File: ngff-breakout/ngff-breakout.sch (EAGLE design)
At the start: 79 parts, among them U1 MIC5366-1.8YC5, U2 MCP1827S-3302E/EB, X1 PINHD-2X4, X10 ZX360D-B-10P(30), X2 692121030100, X3 PINHD-2X10, X4 PINHD-2X5, X5 694108106102, X6 PINHD-1X3, X7 5-1814832-1, X8 5-1814832-1, X9 5-1814832-1, Y1 MHF4, Y2 MHF4, Y3 MHF4

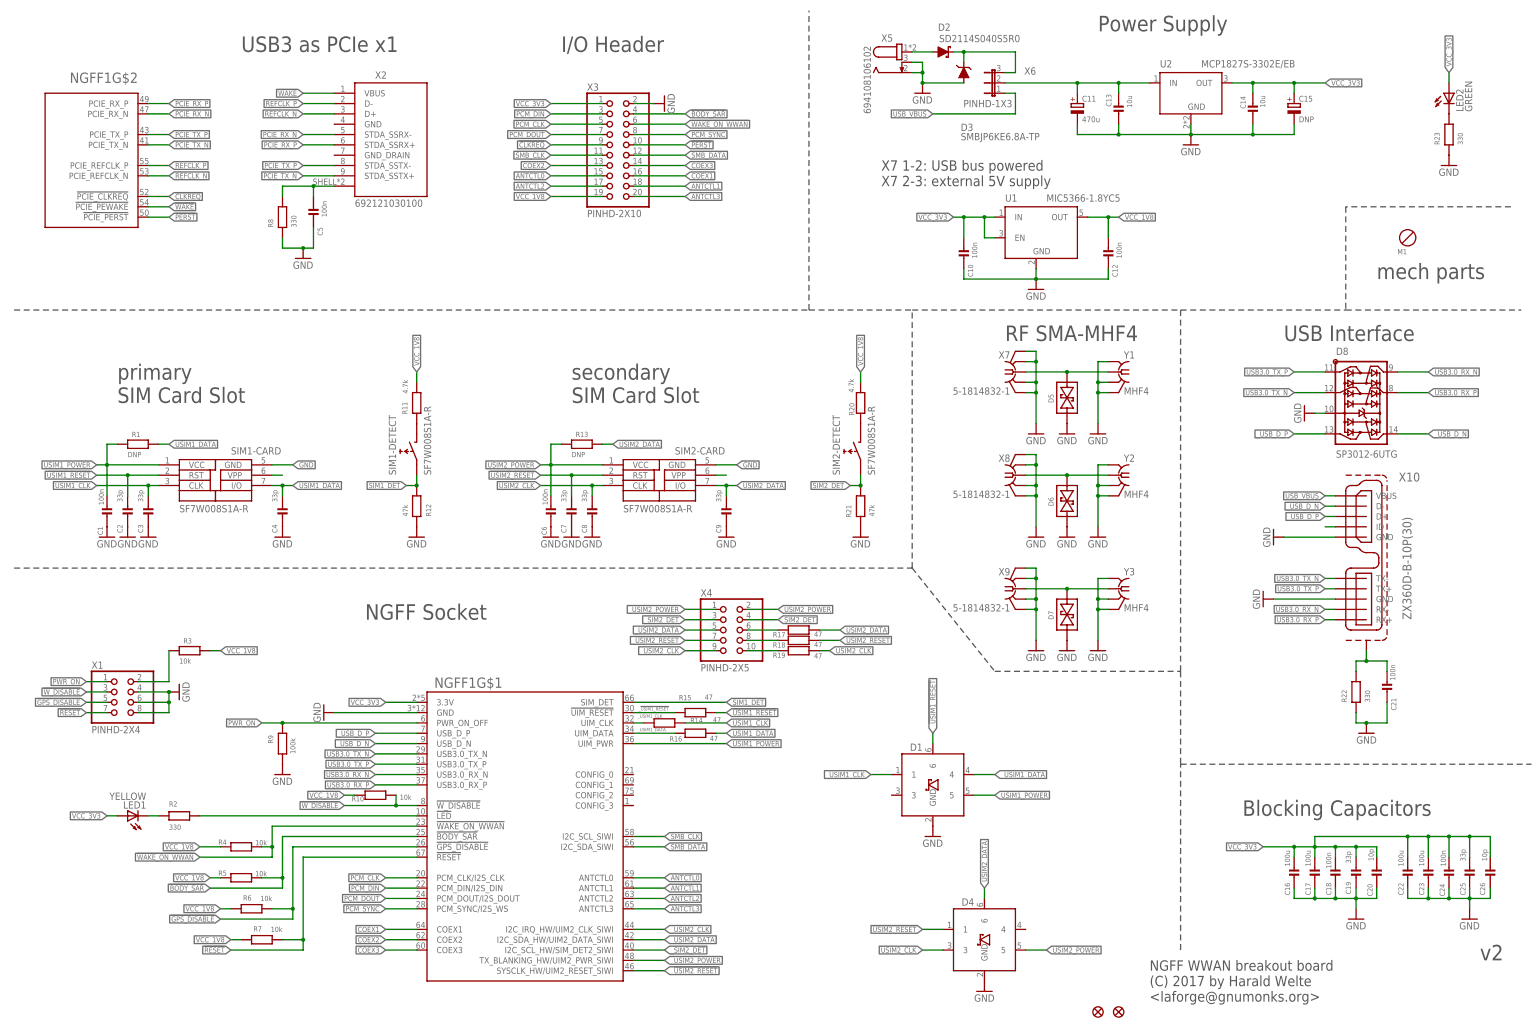
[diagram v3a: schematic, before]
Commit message: ngff: connect pin 4 @X2 to GND (solves OS#4216)
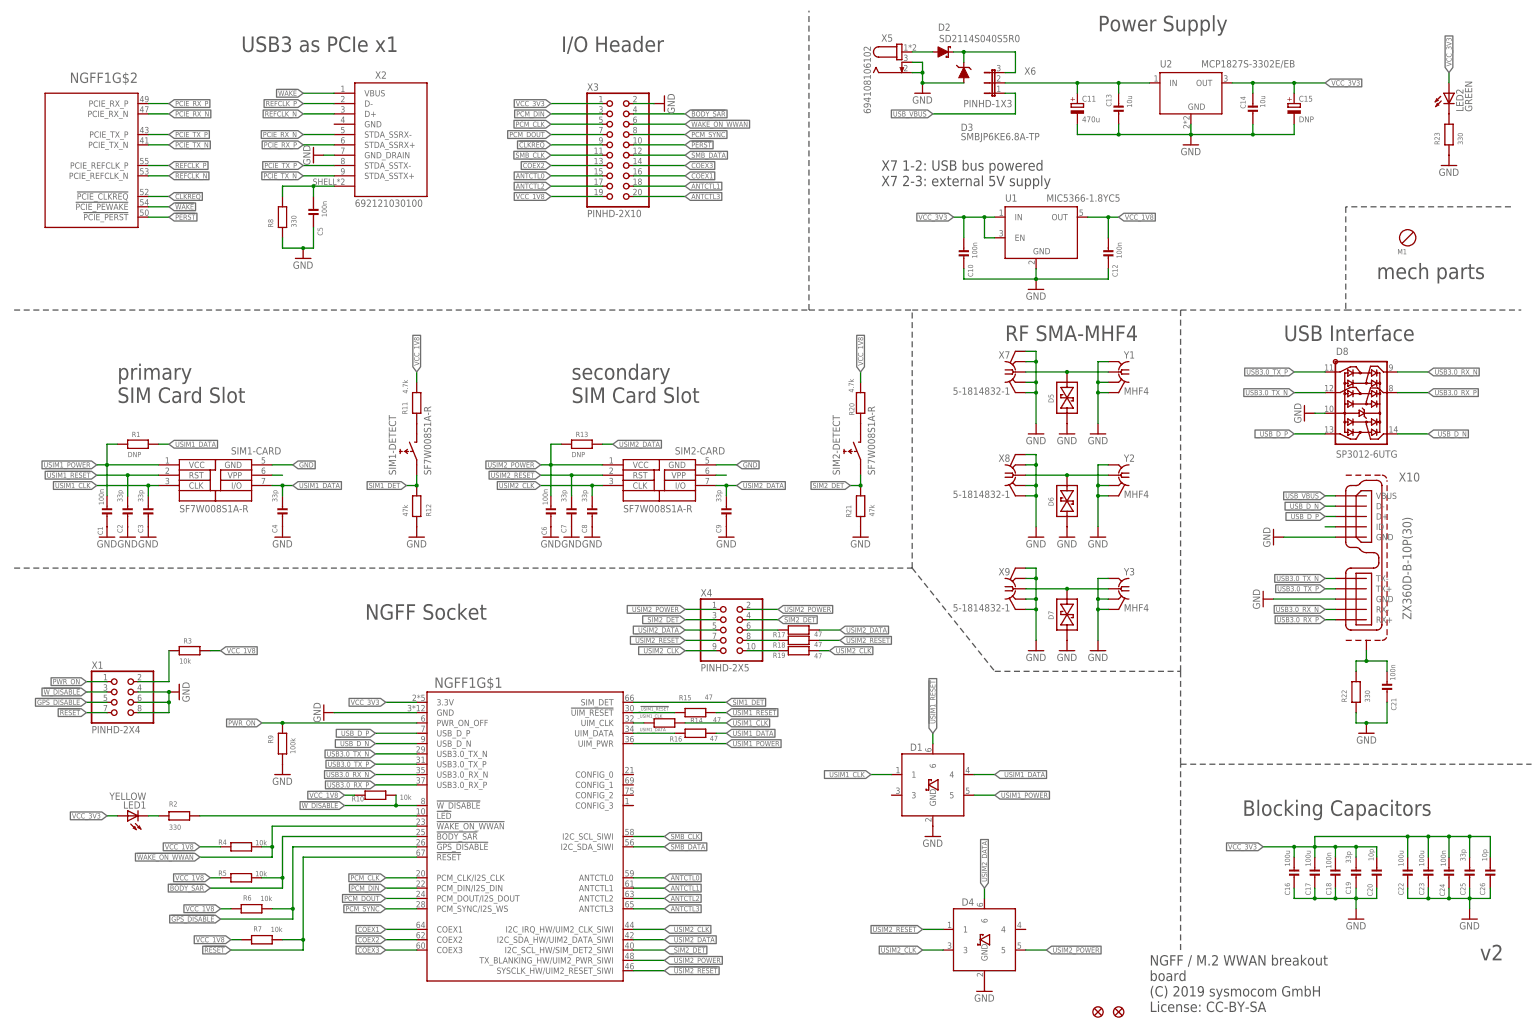
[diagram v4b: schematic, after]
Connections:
- net GND: now also X2.GND_DRAIN
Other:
- note added: "NGFF / M.2 WWAN breakout board (C) 2019 sysmocom GmbH License: CC-BY-SA"
- note removed: "NGFF WWAN breakout board (C) 2017 by Harald Welte <laforge@gnumonks.org>"
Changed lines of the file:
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@@
 <grid distance="0.1" unitdist="inch" unit="inch" style="lines" multiple="1" display="no" altdistance="0.01" altunitdist="inch" altunit="inch"/>
 <layers>
-<layer number="1" name="Top" color="4" fill="1" visible="yes" active="no"/>
-<layer number="2" name="Route2" color="11" fill="3" visible="yes" active="no"/>
-<layer number="3" name="Route3" color="4" fill="3" visible="yes" active="no"/>
-<layer number="4" name="Route4" color="1" fill="4" visible="yes" active="no"/>
-<layer number="5" name="Route5" color="4" fill="4" visible="yes" active="no"/>
-<layer number="6" name="Route6" color="1" fill="8" visible="yes" active="no"/>
-<layer number="7" name="Route7" color="4" fill="8" visible="yes" active="no"/>
-<layer number="8" name="Route8" color="1" fill="2" visible="yes" active="no"/>
-<layer number="9" name="Route9" color="4" fill="2" visible="yes" active="no"/>
-<layer number="10" name="Route10" color="1" fill="7" visible="yes" active="no"/>
-<layer number="11" name="Route11" color="4" fill="7" visible="yes" active="no"/>
-<layer number="12" name="Route12" color="1" fill="5" visible="yes" active="no"/>
-<layer number="13" name="Route13" color="4" fill="5" visible="yes" active="no"/>
-<layer number="14" name="Route14" color="1" fill="6" visible="yes" active="no"/>
-<layer number="15" name="Route15" color="14" fill="6" visible="yes" active="no"/>
-<layer number="16" name="Bottom" color="1" fill="1" visible="yes" active="no"/>
-<layer number="17" name="Pads" color="2" fill="1" visible="yes" active="no"/>
-<layer number="18" name="Vias" color="2" fill="1" visible="yes" active="no"/>
-<layer number="19" name="Unrouted" color="6" fill="1" visible="yes" active="no"/>
-<layer number="20" name="Dimension" color="15" fill="1" visible="yes" active="no"/>
-<layer number="21" name="tPlace" color="7" fill="1" visible="yes" active="no"/>
-<layer number="22" name="bPlace" color="7" fill="1" visible="yes" active="no"/>
-<layer number="23" name="tOrigins" color="15" fill="1" visible="yes" active="no"/>
-<layer number="24" name="bOrigins" color="15" fill="1" visible="yes" active="no"/>
-<layer number="25" name="tNames" color="7" fill="1" visible="yes" active="no"/>
-<layer number="26" name="bNames" color="7" fill="1" visible="yes" active="no"/>
-<layer number="27" name="tValues" color="7" fill="1" visible="yes" active="no"/>
-<layer number="28" name="bValues" color="7" fill="1" visible="yes" active="no"/>
+<layer number="1" name="Top" color="4" fill="1" visible="no" active="no"/>
+<layer number="2" name="Route2" color="11" fill="3" visible="no" active="no"/>
+<layer number="3" name="Route3" color="4" fill="3" visible="no" active="no"/>
+<layer number="4" name="Route4" color="1" fill="4" visible="no" active="no"/>
+<layer number="5" name="Route5" color="4" fill="4" visible="no" active="no"/>
+<layer number="6" name="Route6" color="1" fill="8" visible="no" active="no"/>
+<layer number="7" name="Route7" color="4" fill="8" visible="no" active="no"/>
+<layer number="8" name="Route8" color="1" fill="2" visible="no" active="no"/>
+<layer number="9" name="Route9" color="4" fill="2" visible="no" active="no"/>
+<layer number="10" name="Route10" color="1" fill="7" visible="no" active="no"/>
+<layer number="11" name="Route11" color="4" fill="7" visible="no" active="no"/>
+<layer number="12" name="Route12" color="1" fill="5" visible="no" active="no"/>
+<layer number="13" name="Route13" color="4" fill="5" visible="no" active="no"/>
+<layer number="14" name="Route14" color="1" fill="6" visible="no" active="no"/>
+<layer number="15" name="Route15" color="14" fill="6" visible="no" active="no"/>
+<layer number="16" name="Bottom" color="1" fill="1" visible="no" active="no"/>
+<layer number="17" name="Pads" color="2" fill="1" visible="no" active="no"/>
+<layer number="18" name="Vias" color="2" fill="1" visible="no" active="no"/>
+<layer number="19" name="Unrouted" color="6" fill="1" visible="no" active="no"/>
+<layer number="20" name="Dimension" color="15" fill="1" visible="no" active="no"/>
+<layer number="21" name="tPlace" color="7" fill="1" visible="no" active="no"/>
+<layer number="22" name="bPlace" color="7" fill="1" visible="no" active="no"/>
+<layer number="23" name="tOrigins" color="15" fill="1" visible="no" active="no"/>
+<layer number="24" name="bOrigins" color="15" fill="1" visible="no" active="no"/>
+<layer number="25" name="tNames" color="7" fill="1" visible="no" active="no"/>
+<layer number="26" name="bNames" color="7" fill="1" visible="no" active="no"/>
+<layer number="27" name="tValues" color="7" fill="1" visible="no" active="no"/>
+<layer number="28" name="bValues" color="7" fill="1" visible="no" active="no"/>
 <layer number="29" name="tStop" color="7" fill="3" visible="no" active="no"/>
 <layer number="30" name="bStop" color="7" fill="6" visible="no" active="no"/>
@@
 <layer number="35" name="tGlue" color="7" fill="4" visible="no" active="no"/>
 <layer number="36" name="bGlue" color="7" fill="5" visible="no" active="no"/>
-<layer number="37" name="tTest" color="7" fill="1" visible="yes" active="no"/>
-<layer number="38" name="bTest" color="7" fill="1" visible="yes" active="no"/>
+<layer number="37" name="tTest" color="7" fill="1" visible="no" active="no"/>
+<layer number="38" name="bTest" color="7" fill="1" visible="no" active="no"/>
 <layer number="39" name="tKeepout" color="4" fill="11" visible="no" active="no"/>
 <layer number="40" name="bKeepout" color="1" fill="11" visible="no" active="no"/>
@@
 <layer number="44" name="Drills" color="7" fill="1" visible="no" active="no"/>
 <layer number="45" name="Holes" color="7" fill="1" visible="no" active="no"/>
-<layer number="46" name="Milling" color="3" fill="1" visible="yes" active="no"/>
-<layer number="47" name="Measures" color="7" fill="1" visible="yes" active="no"/>
-<layer number="48" name="Document" color="7" fill="1" visible="yes" active="no"/>
-<layer number="49" name="Reference" color="7" fill="1" visible="yes" active="no"/>
-<layer number="50" name="dxf" color="7" fill="1" visible="yes" active="no"/>
-<layer number="51" name="tDocu" color="7" fill="1" visible="yes" active="no"/>
-<layer number="52" name="bDocu" color="7" fill="1" visible="yes" active="no"/>
-<layer number="53" name="tGND_GNDA" color="7" fill="9" visible="yes" active="no"/>
-<layer number="54" name="bGND_GNDA" color="1" fill="9" visible="yes" active="no"/>
-<layer number="56" name="wert" color="7" fill="1" visible="yes" active="no"/>
-<layer number="57" name="tCAD" color="6" fill="1" visible="yes" active="no"/>
-<layer number="59" name="tMark" color="7" fill="1" visible="yes" active="no"/>
-<layer number="60" name="bMark" color="7" fill="1" visible="yes" active="no"/>
+<layer number="46" name="Milling" color="3" fill="1" visible="no" active="no"/>
+<layer number="47" name="Measures" color="7" fill="1" visible="no" active="no"/>
+<layer number="48" name="Document" color="7" fill="1" visible="no" active="no"/>
+<layer number="49" name="Reference" color="7" fill="1" visible="no" active="no"/>
+<layer number="50" name="dxf" color="7" fill="1" visible="no" active="no"/>
+<layer number="51" name="tDocu" color="7" fill="1" visible="no" active="no"/>
+<layer number="52" name="bDocu" color="7" fill="1" visible="no" active="no"/>
+<layer number="53" name="tGND_GNDA" color="7" fill="9" visible="no" active="no"/>
+<layer number="54" name="bGND_GNDA" color="1" fill="9" visible="no" active="no"/>
+<layer number="56" name="wert" color="7" fill="1" visible="no" active="no"/>
+<layer number="57" name="tCAD" color="6" fill="1" visible="no" active="no"/>
+<layer number="59" name="tMark" color="7" fill="1" visible="no" active="no"/>
+<layer number="60" name="bMark" color="7" fill="1" visible="no" active="no"/>
 <layer number="90" name="Modules" color="5" fill="1" visible="yes" active="yes"/>
 <layer number="91" name="Nets" color="2" fill="1" visible="yes" active="yes"/>
@@
 <attribute name="SOURCEPARTNUMBER" value="UNKNOWN SOURCE PART NUMBER"/>
 </part>
+<part name="GND29" library="supply1" deviceset="GND" device=""/>
 </parts>
 <sheets>
 <sheet>
 <plain>
-<text x="289.56" y="10.16" size="2.54" layer="97">NGFF WWAN breakout board
-(C) 2017 by Harald Welte
-&lt;laforge@gnumonks.org&gt;</text>
+<text x="289.56" y="7.62" size="2.54" layer="97">NGFF / M.2 WWAN breakout
+board
+(C) 2019 sysmocom GmbH
+License: CC-BY-SA</text>
 <wire x1="10.16" y1="180.34" x2="205.74" y2="180.34" width="0.1524" layer="97" style="longdash"/>
 <wire x1="205.74" y1="180.34" x2="205.74" y2="254" width="0.1524" layer="97" style="longdash"/>
@@
 <attribute name="LINK" x="185.42" y="101.6" size="1.778" layer="96" display="off"/>
 </instance>
+<instance part="GND29" gate="1" x="83.82" y="218.44" rot="R270"/>
 </instances>
 <busses>
@@
 <pinref part="GND28" gate="1" pin="GND"/>
 </segment>
+<segment>
+<pinref part="X2" gate="G$1" pin="GND_DRAIN"/>
+<pinref part="GND29" gate="1" pin="GND"/>
+<wire x1="86.36" y1="218.44" x2="88.9" y2="218.44" width="0.1524" layer="91"/>
+</segment>
 </net>
